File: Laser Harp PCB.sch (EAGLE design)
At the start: 35 parts, among them J1 DCJ0202, X1 22-23-2021, X10 22-23-2051, X11 22-23-2021, X12 22-23-2021, X2 22-23-2021, X3 22-23-2021, X4 22-23-2021, X5 22-23-2021, X6 22-23-2021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

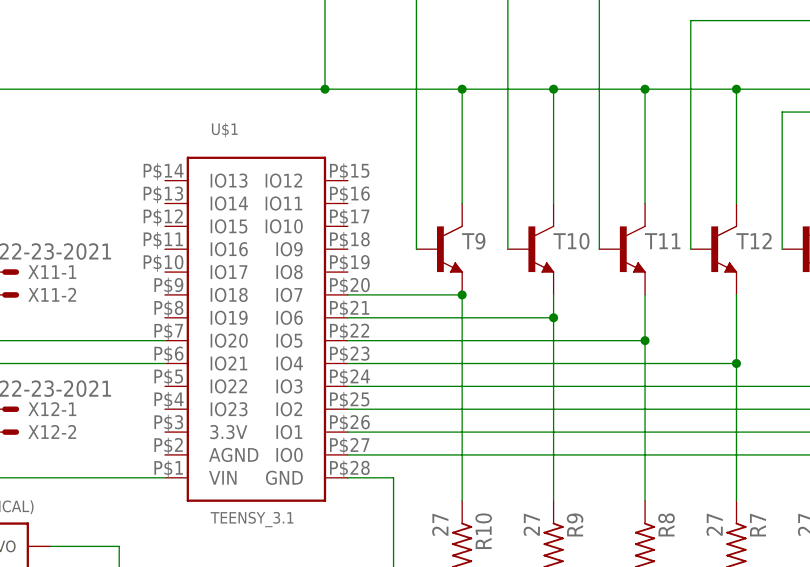
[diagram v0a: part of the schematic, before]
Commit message: Updated pin connection
The BJTs used to connect to pins 0 through 7 of the Teensy, but the Audio Shield uses pin 7 to transmit information from the micro sd card to the Teensy. I changed the connection from pin 7 to pin 8.
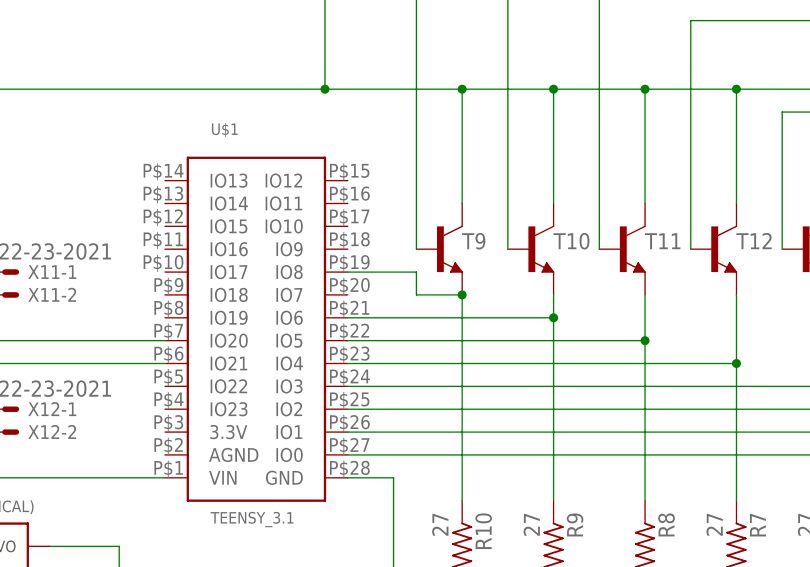
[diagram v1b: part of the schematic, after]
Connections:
- net N$24: now also U$1.IO8; no longer U$1.IO7
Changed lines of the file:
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@@
 <net name="N$24" class="0">
 <segment>
-<pinref part="U$1" gate="G$1" pin="IO7"/>
-<wire x1="116.84" y1="116.84" x2="129.54" y2="116.84" width="0.1524" layer="91"/>
 <pinref part="T9" gate="G$1" pin="E"/>
 <pinref part="R10" gate="G$1" pin="1"/>
+<wire x1="124.46" y1="116.84" x2="129.54" y2="116.84" width="0.1524" layer="91"/>
 <wire x1="129.54" y1="116.84" x2="129.54" y2="93.98" width="0.1524" layer="91"/>
 <junction x="129.54" y="116.84"/>
+<pinref part="U$1" gate="G$1" pin="IO8"/>
+<wire x1="116.84" y1="119.38" x2="124.46" y2="119.38" width="0.1524" layer="91"/>
+<wire x1="124.46" y1="119.38" x2="124.46" y2="116.84" width="0.1524" layer="91"/>
 </segment>
 </net>
